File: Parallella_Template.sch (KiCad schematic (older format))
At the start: 4 parts, among them J11 BTH-030-XX-X-D, J13 BTH-030-XX-X-D, J8 BTH-030-XX-X-D, J9 BTH-030-XX-X-D

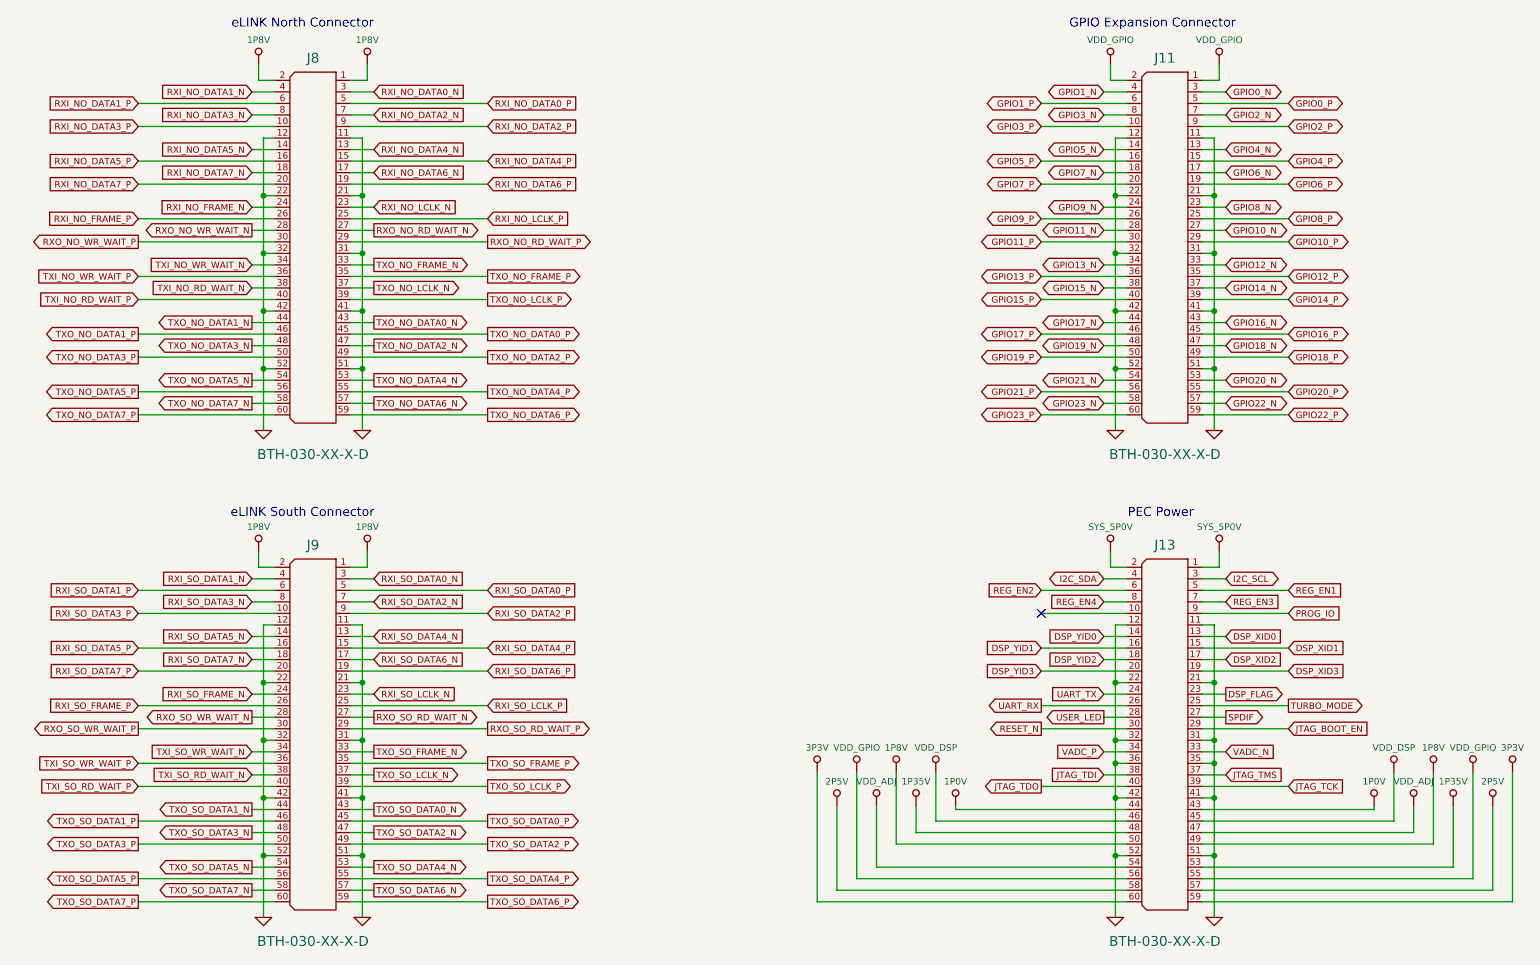
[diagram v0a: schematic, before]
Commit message: Created hierarchy in schematic. Final connectors layout.
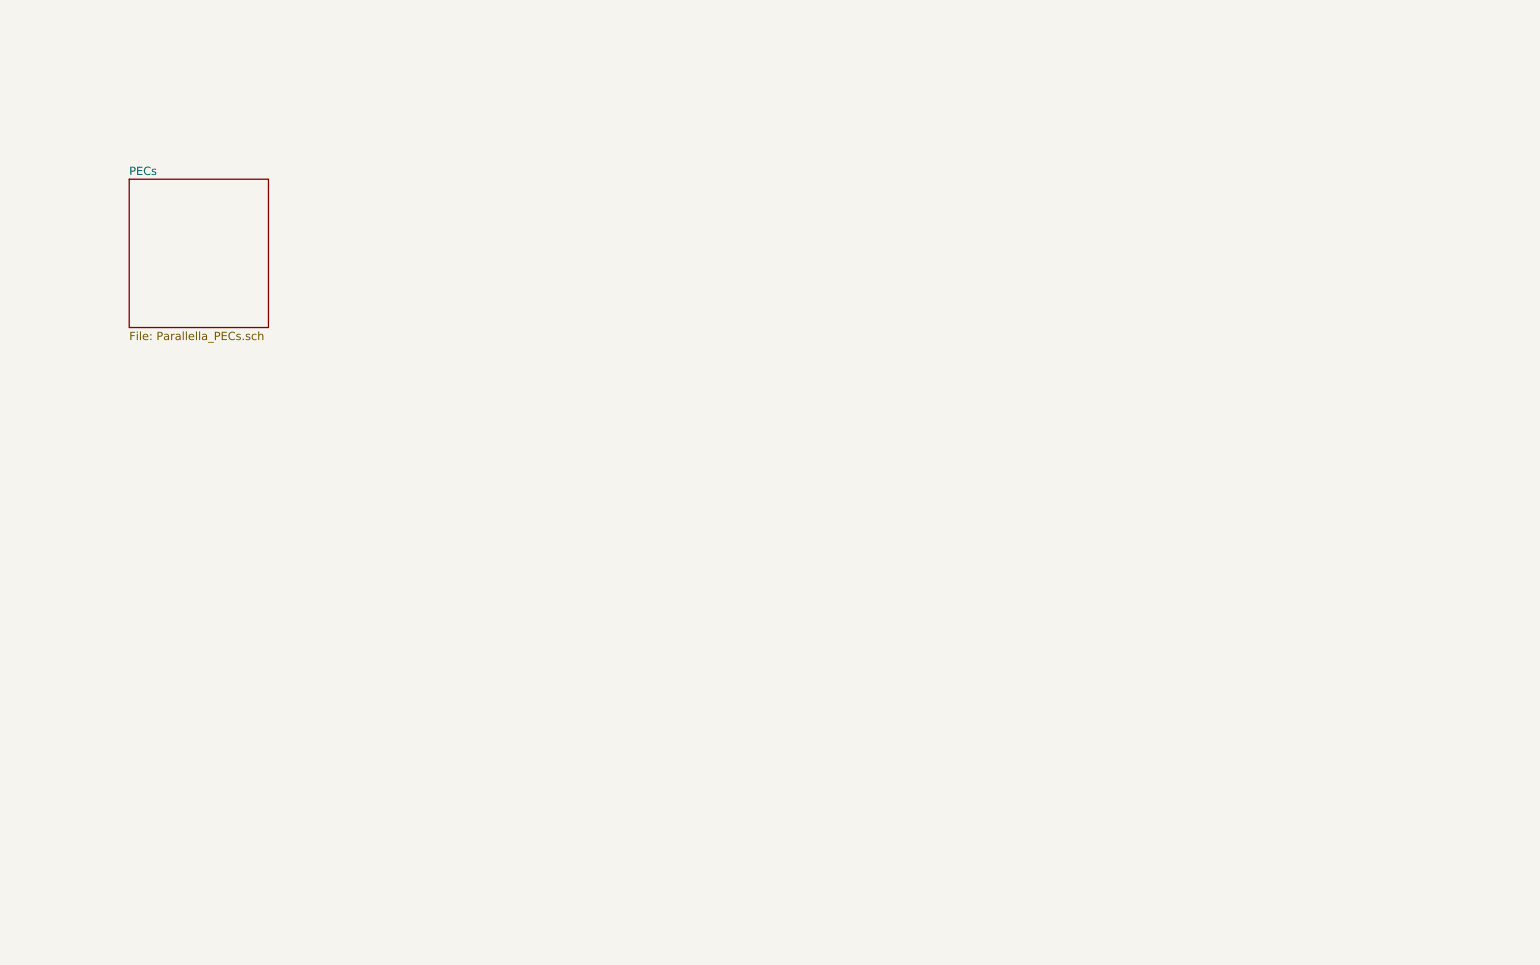
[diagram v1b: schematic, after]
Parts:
- removed J11, J13, J8, J9: BTH-030-XX-X-D, symbol BTH-030-XX-X-D
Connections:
- no-connect marks 1 -> 0
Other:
- note removed: "GPIO Expansion Connector"
- note removed: "PEC Power"
- note removed: "eLINK North Connector"
- note removed: "eLINK South Connector"
